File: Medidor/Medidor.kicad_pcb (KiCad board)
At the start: 2 copper layers, 34 parts

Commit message: Add files via upload
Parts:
- added D1: LED, LED_SMD:LED_0603_1608Metric, F.Cu at (145.3, 62.3)
- added J1: TC2030-CTX-TAG_CONECT, Connector:Tag-Connect_TC2030-IDC-NL_2x03_P1.27mm_Vertical, F.Cu at (172.7, 43.2)
- added SW1: Rotary_Encoder_Switch, Rotary_Encoder:RotaryEncoder_Alps_EC11E-Switch_Vertical_H20mm, F.Cu at (119.6, 55.4)
- added U1: INA219-INA, Package_TO_SOT_SMD:SuperSOT-8, F.Cu at (99.1, 45.7)
- added dc1: DC-DC, Package_TO_SOT_SMD:SuperSOT-8, F.Cu at (144.8, 52.1)
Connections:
- net Rx renamed /RX
- net Tx renamed /TX
- R14 pad 2: Net-(R14-Pad2) -> /R_B

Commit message: Placement in progress
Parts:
- removed R4, R5: 1kΩ, Resistor_SMD:R_0402_1005Metric
- added Fil1: 2450FM07A0029T, Medidor:baloon, F.Cu at (156.8, 110.9)
- added R1: Shunt, Resistor_SMD:R_0805_2012Metric, F.Cu at (187.4, 107.8)
- added SW2: SW_DPST_x2, Medidor:botao, F.Cu at (142.4, 126.1)
- added U2: Serial, Connector:FanPinHeader_1x03_P2.54mm_Vertical, F.Cu at (134.7, 122.8)
- added U3: 2450AT18D0100, Medidor:2450AT18D0100, F.Cu at (164.1, 123.6)
- added X1: 32MHz, Medidor:cristal, F.Cu at (161.4, 106.0)
- moved C16 107.2 mm to (58.7, 118.4), turned to 90 degrees
- moved dc1 101.4 mm to (67.6, 117.8), turned to 180 degrees
- moved U1 98.2 mm to (175.8, 106.9), turned to 180 degrees
- moved C12 91.9 mm to (75.2, 119.2), turned to 90 degrees
- moved J1 78.5 mm to (158.4, 120.4), turned to 270 degrees
- moved SW1 67.1 mm to (116.5, 122.4), turned to 90 degrees
- moved C14 66.8 mm to (113.9, 127.7), turned to 270 degrees
- moved R11 66.6 mm to (124.2, 126.9)
- moved C15 65.0 mm to (127.1, 127.7), turned to 270 degrees
- moved R10 52.0 mm to (115.3, 126.1)
- moved R14 51.1 mm to (121.6, 104.9), turned to 270 degrees
- moved R12 49.6 mm to (127.3, 124.2), turned to 270 degrees
- moved D1 49.4 mm to (136.5, 110.9), turned to 90 degrees
- moved C8 47.6 mm to (146.0, 114.5), turned to 90 degrees
- moved R16 39.9 mm to (184.2, 107.3), turned to 180 degrees
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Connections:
- C14 pad 1: AIN1 -> RC1
- C15 pad 1: AIN0 -> RC2
- MCU1 pad 4: AIN0 -> RC3
- MCU1 pad 5: AIN1 -> RC2
- MCU1 pad 6: Net-(MCU1-Pad6) -> RC1
- R10 pad 1: AIN1 -> RC1
- R11 pad 2: AIN0 -> RC2
- R12 pad 2: AIN0 -> RC2
- R14 pad 2: /R_B -> RC3
- R8 pad 1: /RF -> Net-(R8-Pad1)
- R9 pad 2: AIN1 -> RC1
- SW1 pad S1: /R_B -> RC3
- U1 pad 7: Net-(R5-Pad2) -> Earth
- U1 pad 8: Net-(R4-Pad2) -> Earth
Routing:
- net +3V3: track 0.00 -> 42.1 mm
- net Earth: track 0.00 -> 31.5 mm, vias 0 -> 24
- net nRESET: track 0.00 -> 14.9 mm
- net SWDCLK: track 0.00 -> 11.5 mm, vias 0 -> 2
- net SWDIO: track 0.00 -> 10.3 mm
- net Net-(C1-Pad2): track 0.00 -> 9.73 mm
- net +5V: track 0.00 -> 7.04 mm
- net Net-(C2-Pad2): track 0.00 -> 6.04 mm
- net Net-(C4-Pad2): track 0.00 -> 5.96 mm
- net Net-(C5-Pad1): track 0.00 -> 5.74 mm
- net Net-(C5-Pad2): track 0.00 -> 5.69 mm
- net Net-(R11-Pad1): track 0.00 -> 5.36 mm
- net RC2: track 0.00 -> 5.20 mm
- net SDA: track 0.00 -> 3.47 mm
- net SCL: track 0.00 -> 3.34 mm
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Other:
- net class Default: clearance 0.2 -> 0.1; trace_width 0.25 -> 0.2; via_dia 0.8 -> 0.5; via_drill 0.4 -> 0.3
- net class Suply added: clearance 0.1, trace_width 0.4, via_dia 0.8, via_drill 0.5
- rule trace_clearance: 0.2 -> 0.1

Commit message: Replacement
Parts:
- R7: value 1k -> 0
- moved R9 67.9 mm to (128.4, 104.2), turned to 90 degrees
- moved SW2 62.7 mm to (79.7, 126.8)
- moved J1 47.1 mm to (111.6, 125.0), turned to 180 degrees
- moved U2 41.3 mm to (93.5, 123.8)
- moved R7 40.6 mm to (132.0, 128.2), turned to 270 degrees
- moved R8 39.0 mm to (133.6, 128.7)
- moved R6 38.4 mm to (133.6, 127.6), turned to 0 degrees
- moved C13 37.9 mm to (133.5, 121.6), turned to 270 degrees
- moved U3 34.1 mm to (130.5, 129.3), turned to 180 degrees
- moved C15 32.9 mm to (129.6, 94.9), turned to 90 degrees
- moved R1 32.2 mm to (157.3, 119.2)
- moved R15 32.2 mm to (154.1, 119.7)
- moved R16 32.2 mm to (154.1, 118.7)
- moved C5 31.2 mm to (151.9, 119.2)
- moved R11 30.2 mm to (128.3, 97.0), turned to 90 degrees
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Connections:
- C1 pad 1: Earth -> GND
- C10 pad 1: Earth -> GND
- C11 pad 1: Earth -> GND
- C12 pad 2: Earth -> GND
- C13 pad 2: Earth -> GND
- C14 pad 2: Earth -> GND
- C15 pad 2: Earth -> GND
- C16 pad 2: Earth -> GND
- C2 pad 1: Earth -> GND
- C3 pad 1: Earth -> GND
- C4 pad 1: Earth -> GND
- C7 pad 1: Earth -> GND
- C8 pad 1: Earth -> GND
- C9 pad 1: Earth -> GND
- Display1 pad 1: Earth -> GND
- Fil1 pad 2: Earth -> GND
- Fil1 pad 4: Earth -> GND
- J1 pad 5: Earth -> GND
- MCU1 pad 31: Earth -> GND
- MCU1 pad 45: Earth -> GND
- MCU1 pad 49: Earth -> GND
- R6 pad 2: Earth -> GND
- R8 pad 1: Net-(R8-Pad1) -> /RF
- R8 pad 2: Earth -> GND
- SW1 pad C: Earth -> GND
- SW1 pad S2: Earth -> GND
- SW2 pad 1: Earth -> GND
- U1 pad 3: Earth -> GND
- U1 pad 7: Earth -> GND
- U1 pad 8: Earth -> GND
- U2 pad 1: (no net) -> GND
- U2 pad 2: (no net) -> /TX
- U2 pad 3: (no net) -> /RX
- U3 pad 2: Earth -> GND
- U3 pad 3: Earth -> GND
- U3 pad 4: Net-(R8-Pad1) -> GND
- dc1 pad 2: Earth -> GND
- dc1 pad 3: Earth -> GND
- dc1 pad 6: Earth -> GND
- dc1 pad 7: Earth -> GND
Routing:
- net +3V3: track 42.1 -> 0.06 mm
- net Earth: track 31.5 -> 0.00 mm, vias 24 -> 0
- net nRESET: track 14.9 -> 0.00 mm
- net SWDCLK: track 11.5 -> 0.00 mm, vias 2 -> 0
- net SWDIO: track 10.3 -> 0.00 mm
- net Net-(C1-Pad2): track 9.73 -> 0.00 mm
- net +5V: track 7.04 -> 0.00 mm
- net Net-(C2-Pad2): track 6.04 -> 0.00 mm
- net Net-(C4-Pad2): track 5.96 -> 0.00 mm
- net Net-(C5-Pad2): track 5.69 -> 0.03 mm
- net Net-(C5-Pad1): track 5.74 -> 0.12 mm
- net Net-(R11-Pad1): track 5.36 -> 0.00 mm
- net RC2: track 5.20 -> 0.00 mm
- net SDA: track 3.47 -> 0.00 mm
- net SCL: track 3.34 -> 0.00 mm
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- added copper zone on B.Cu, net GND
- added copper zone on F.Cu, net GND
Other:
- board outline added: 93.3 x 43.8 mm

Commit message: Add files via upload
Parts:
- removed Display1: OLED, Medidor:OLED
- added Display: OLED, Medidor:OLED, F.Cu at (91.9, 103.1)
- added Screw_Terminal: TerminalBlock_Altech_AK300-2_P5.00mm, TerminalBlock:TerminalBlock_Altech_AK300-2_P5.00mm, F.Cu at (139.4, 106.2)
- added USB: USB_Micro-B_Wuerth_629105150521_CircularHoles, Connector_USB:USB_Micro-B_Wuerth_629105150521_CircularHoles, F.Cu at (73.7, 123.7)
- moved C3 15.5 mm to (125.7, 114.6)
- moved MCU1 15.5 mm to (116.7, 116.1)
- moved R7 15.5 mm to (116.5, 128.2)
- moved X1 15.5 mm to (124.5, 121.4)
- moved C11 15.5 mm to (135.5, 115.0)
- moved C13 15.5 mm to (118.0, 121.6)
- moved C2 15.5 mm to (122.5, 124.8)
- moved C4 15.5 mm to (119.1, 121.6)
- moved C5 15.5 mm to (136.4, 119.2)
- moved C7 15.5 mm to (120.3, 110.6)
- moved C8 15.5 mm to (111.9, 112.9)
- moved Fil1 15.5 mm to (116.3, 120.8)
- moved L1 15.5 mm to (123.0, 113.3)
- moved R1 15.5 mm to (141.8, 119.2)
- moved R15 15.5 mm to (138.6, 119.7)
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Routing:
- net Net-(R1-Pad1): track 0.61 -> 0.00 mm
- net Net-(R1-Pad2): track 0.52 -> 0.00 mm
- removed copper zone on B.Cu, net GND
- removed copper zone on F.Cu, net GND
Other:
- board size 93.3 x 43.8 mm -> 79 x 43.8 mm

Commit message: Add files via upload
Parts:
- moved Screw_Terminal 3.88 mm to (141.5, 109.5), turned to 90 degrees
- renumbered U2 to UART, dc1 to dc-dc
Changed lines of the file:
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@@
   )
   (module TerminalBlock:TerminalBlock_Altech_AK300-2_P5.00mm (layer F.Cu)
-    (at 139.446 106.172)
+    (at 141.478 109.474 90)
     (descr "Altech AK300 terminal block, pitch 5.0mm, 45 degree angled, see http://www.mouser.com/ds/2/16/PCBMETRC-24178.pdf")
     (tags "Altech AK300 terminal block pitch 5.0mm")
-    (fp_text reference Screw_Terminal (at 2.032 -7.874) (layer F.SilkS)
-      (effects (font (size 1 1) (thickness 0.15)))
-    )
-    (fp_text value TerminalBlock_Altech_AK300-2_P5.00mm (at 2.78 7.75) (layer F.Fab)
-      (effects (font (size 1 1) (thickness 0.15)))
-    )
-    (fp_text user %R (at 2.5 -2) (layer F.Fab)
+    (fp_text reference Screw_Terminal (at 9.398 -0.254 180) (layer F.SilkS)
+      (effects (font (size 1 1) (thickness 0.15)))
+    )
+    (fp_text value TerminalBlock_Altech_AK300-2_P5.00mm (at 2.78 7.75 90) (layer F.Fab)
+      (effects (font (size 1 1) (thickness 0.15)))
+    )
+    (fp_text user %R (at 2.5 -2 90) (layer F.Fab)
       (effects (font (size 1 1) (thickness 0.15)))
     )
@@
     (fp_arc (start -0.01 -3.71) (end -1.62 -5) (angle 100) (layer F.Fab) (width 0.1))
     (fp_arc (start -1.13 -4.65) (end -1.42 -4.13) (angle 104.2) (layer F.Fab) (width 0.1))
-    (pad 1 thru_hole rect (at 0 0) (size 1.98 3.96) (drill 1.32) (layers *.Cu *.Mask))
-    (pad 2 thru_hole oval (at 5 0) (size 1.98 3.96) (drill 1.32) (layers *.Cu *.Mask))
+    (pad 1 thru_hole rect (at 0 0 90) (size 1.98 3.96) (drill 1.32) (layers *.Cu *.Mask))
+    (pad 2 thru_hole oval (at 5 0 90) (size 1.98 3.96) (drill 1.32) (layers *.Cu *.Mask))
     (model ${KISYS3DMOD}/TerminalBlock.3dshapes/TerminalBlock_Altech_AK300-2_P5.00mm.wrl
       (at (xyz 0 0 0))
@@
     (tags resistor)
     (attr smd)
-    (fp_text reference R14 (at 0 -1.17 90) (layer F.SilkS)
+    (fp_text reference R14 (at 0.531 1.27 270) (layer F.SilkS)
       (effects (font (size 1 1) (thickness 0.15)))
     )
@@
     (tags "SuperSOT-8 SSOT-8")
     (attr smd)
-    (fp_text reference dc1 (at 0 -2.95 90) (layer F.SilkS)
+    (fp_text reference dc-dc (at 0 -2.95 90) (layer F.SilkS)
       (effects (font (size 1 1) (thickness 0.15)))
     )
@@
     (descr "3-pin CPU fan Through hole pin header, see http://www.formfactors.org/developer%5Cspecs%5Crev1_2_public.pdf")
     (tags "pin header 3-pin CPU fan")
-    (fp_text reference U2 (at 2.54 5.08) (layer F.SilkS) hide
-      (effects (font (size 1 1) (thickness 0.15)))
-    )
+    (fp_text reference UART (at 2.54 5.08) (layer B.SilkS) hide
+      (effects (font (size 1 1) (thickness 0.15)))
+    )

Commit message: Add files via upload
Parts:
- removed U1: INA219-INA, Package_TO_SOT_SMD:SuperSOT-8
- removed dc-dc: DC-DC, Package_TO_SOT_SMD:SuperSOT-8
- added  L78L: L78L, Medidor:L78L, F.Cu at (94.7, 100.1)
- added INA219: INA219, Medidor:INA219, F.Cu at (126.7, 108.7)
- added U10: spacer, Medidor:spacer, F.Cu at (85.5, 90.4)
- added U4: Fiducial, Fiducial:Fiducial_0.75mm_Mask1.5mm, F.Cu at (128.6, 90.2)
- added U5: Fiducial, Fiducial:Fiducial_0.75mm_Mask1.5mm, F.Cu at (139.6, 130.1)
- added U6: Fiducial, Fiducial:Fiducial_0.75mm_Mask1.5mm, F.Cu at (87.4, 128.8)
- added U7: spacer, Medidor:spacer, F.Cu at (140.9, 90.1)
- added U8: spacer, Medidor:spacer, F.Cu at (140.6, 134.2)
- added U9: spacer, Medidor:spacer, F.Cu at (85.6, 133.9)
- Display, SW1, SW2, Screw_Terminal, USB: moved to B.Cu
- U2: renamed from UART; moved to B.Cu
- moved U2 42.7 mm to (136.7, 124.8), turned to 90 degrees
- moved C15 39.8 mm to (124.1, 132.4), turned to 270 degrees
- moved R12 39.8 mm to (122.9, 132.4), turned to 90 degrees
- moved R14 39.4 mm to (103.1, 128.8)
- moved R11 35.1 mm to (122.9, 130.2), turned to 270 degrees
- moved U3 31.1 mm to (85.4, 119.8), turned to 90 degrees
- moved USB 28.0 mm to (87.4, 99.3), turned to 90 degrees
- moved R13 26.6 mm to (128.4, 125.4), turned to 270 degrees
- moved R10 24.6 mm to (122.7, 123.3), turned to 270 degrees
- moved SW1 23.3 mm to (120.1, 124.0)
- moved C16 21.9 mm to (94.7, 93.2)
- moved C12 21.9 mm to (94.7, 106.9)
- moved J1 21.4 mm to (105.5, 101.9), turned to 0 degrees
- moved Display 20.8 mm to (112.8, 103.6), turned to 180 degrees
- moved C2 20.4 mm to (104.6, 115.1), turned to 90 degrees
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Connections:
- MCU1 pad 15: /TX -> Net-(MCU1-Pad15)
- MCU1 pad 16: /RX -> Net-(MCU1-Pad16)
- MCU1 pad 3: Net-(MCU1-Pad3) -> /TX
- MCU1 pad 38: Net-(MCU1-Pad38) -> RC1
- MCU1 pad 39: Net-(MCU1-Pad39) -> RC2
- MCU1 pad 4: RC3 -> /RX
- MCU1 pad 42: SDA -> LEDMCU
- MCU1 pad 43: SCL -> RC3
- MCU1 pad 5: RC2 -> Net-(MCU1-Pad5)
- MCU1 pad 6: RC1 -> Net-(MCU1-Pad6)
- MCU1 pad 8: LEDMCU -> SDA
- MCU1 pad 9: Net-(MCU1-Pad9) -> SCL
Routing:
- net RC3: track 0.00 -> 2.64 mm
- net GND: vias 9 -> 0
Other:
- board size 79 x 43.8 mm -> 58.9 x 47.1 mm

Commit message: conexões
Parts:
- moved R8 12.1 mm to (89.2, 116.9), turned to 270 degrees
- moved R7 8.71 mm to (90.9, 116.5), turned to 180 degrees
- moved R6 8.34 mm to (92.8, 116.9), turned to 270 degrees
- moved D1 6.30 mm to (128.2, 128.0)
- moved C12 4.36 mm to (90.4, 107.6), turned to 180 degrees
- moved R13 3.39 mm to (129.7, 128.5), turned to 90 degrees
- moved U3 3.24 mm to (85.4, 116.6)
- moved R16 2.92 mm to (131.7, 110.2)
- moved R15 2.92 mm to (131.7, 111.3)
- moved R1 2.92 mm to (133.7, 111.0)
- moved C5 2.86 mm to (130.2, 110.7)
- moved SW2 2.54 mm to (92.1, 120.7)
- moved C8 2.03 mm to (116.2, 104.3), turned to 180 degrees
- moved U8 1.23 mm to (141.9, 134.2)
- moved INA219 1.13 mm to (125.9, 109.4)
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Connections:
- MCU1 pad 38: RC1 -> RC3
- MCU1 pad 42: LEDMCU -> RC1
- MCU1 pad 43: RC3 -> LEDMCU
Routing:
- net +3V3: track 0.00 -> 98.4 mm, vias 0 -> 31
- net RC2: track 0.00 -> 34.0 mm
- net (no net): track 0.00 -> 28.0 mm, vias 0 -> 4
- net RC1: track 0.00 -> 27.4 mm
- net /TX: track 0.00 -> 26.5 mm
- net SDA: track 0.00 -> 25.6 mm, vias 0 -> 2
- net /RX: track 0.00 -> 24.4 mm
- net SCL: track 0.00 -> 24.1 mm
- net LEDMCU: track 0.00 -> 22.9 mm, vias 0 -> 2
- net RC3: track 2.64 -> 23.6 mm
- net nRESET: track 0.00 -> 21.0 mm, vias 0 -> 5
- net Net-(Fil1-Pad3): track 0.00 -> 19.7 mm
- net SWDIO: track 0.00 -> 16.1 mm
- net GND: track 0.00 -> 14.8 mm, vias 0 -> 297
- net SWDCLK: track 0.00 -> 12.4 mm
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- added copper zone on B.Cu, net +3V3
- added copper zone on F.Cu, net +3V3
- added copper zone on B.Cu, net +5V
- added copper zone on F.Cu, net +5V
- added copper zone on B.Cu, net GND
- added copper zone on F.Cu, net GND
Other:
- board size 58.9 x 47.1 mm -> 59.9 x 47.1 mm
- net class Ant added: clearance 0.1, trace_width 1.2, via_dia 0.5, via_drill 0.3
- board text added: "GND"

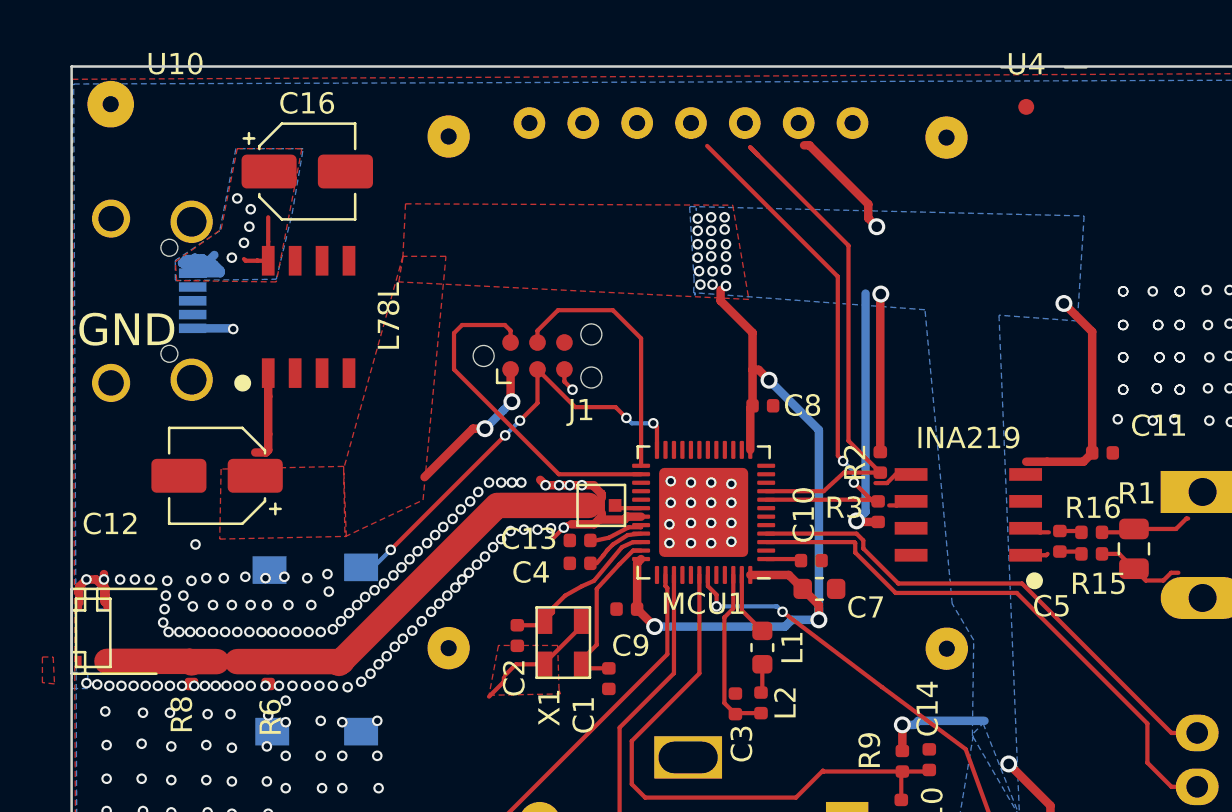
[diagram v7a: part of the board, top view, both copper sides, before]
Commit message: Footprints USB, DISPLAY, INA219 E L78L associados
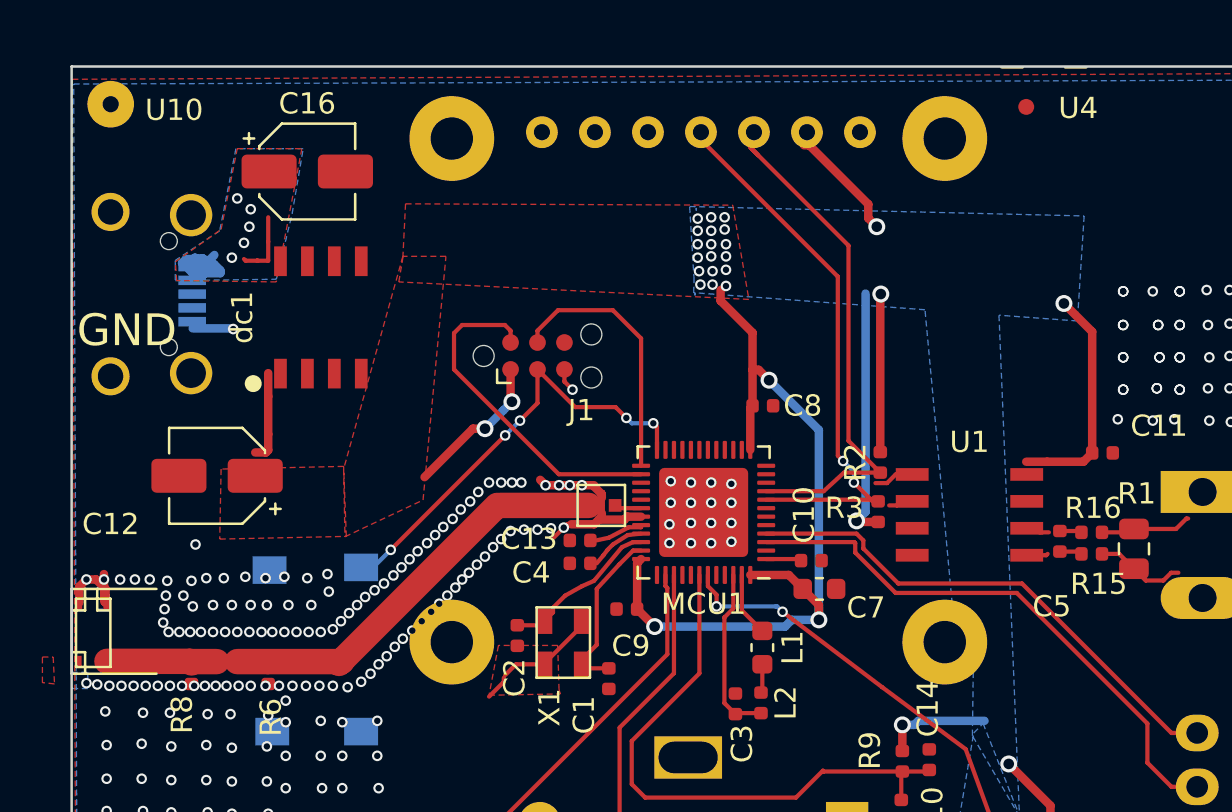
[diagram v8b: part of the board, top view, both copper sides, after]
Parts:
- removed  L78L: L78L, Medidor:L78L
- removed Display: OLED, Medidor:OLED
- removed INA219: INA219, Medidor:INA219
- removed USB: USB_Micro-B_Wuerth_629105150521_CircularHoles, Connector_USB:USB_Micro-B_Wuerth_629105150521_CircularHoles
- added Display1: OLED, Medidor:OLED, B.Cu at (126.7, 89.7)
- added U1: INA219-INA, Medidor:INA219, F.Cu at (125.9, 109.4)
- added US1: USB, Connector_USB:USB_Micro-B_Wuerth_629105150521_CircularHoles, B.Cu at (87.3, 99.0)
- added dc1: DC-DC, Medidor:L78L, F.Cu at (95.3, 100.1)
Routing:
- net (no net): track 28.0 -> 14.3 mm, vias 4 -> 8
- net GND: track 14.8 -> 23.3 mm, vias 297 -> 293
- net SCL: track 24.1 -> 26.0 mm
- net Net-(C5-Pad1): track 1.04 -> 2.22 mm
- net SDA: track 25.6 -> 26.7 mm
- net Net-(C5-Pad2): track 1.06 -> 2.13 mm
